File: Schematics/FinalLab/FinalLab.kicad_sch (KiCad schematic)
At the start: 0 parts

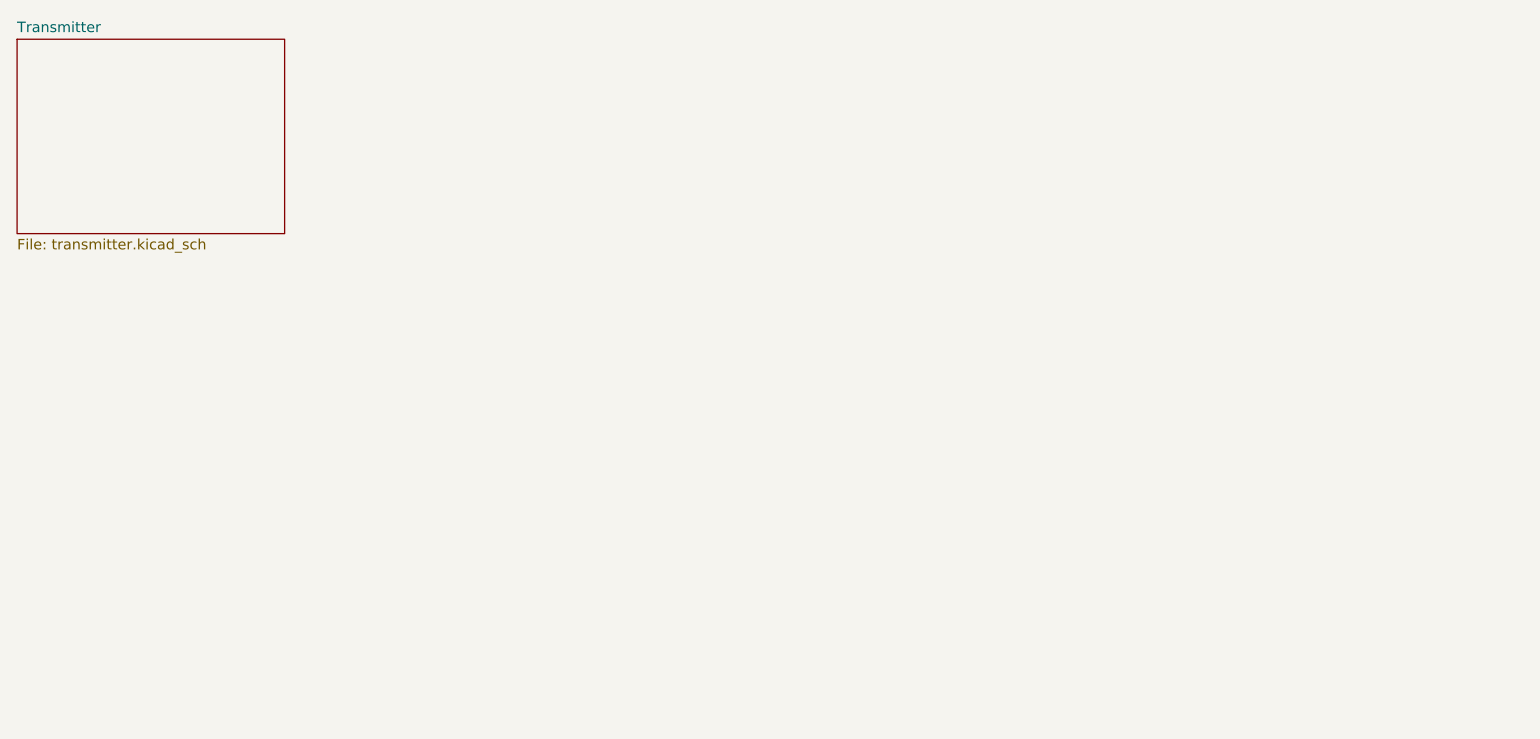
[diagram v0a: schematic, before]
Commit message: WIP
Labview is being worked on, schematic is complete, report is almost done. We need reciever code with PID stuff.
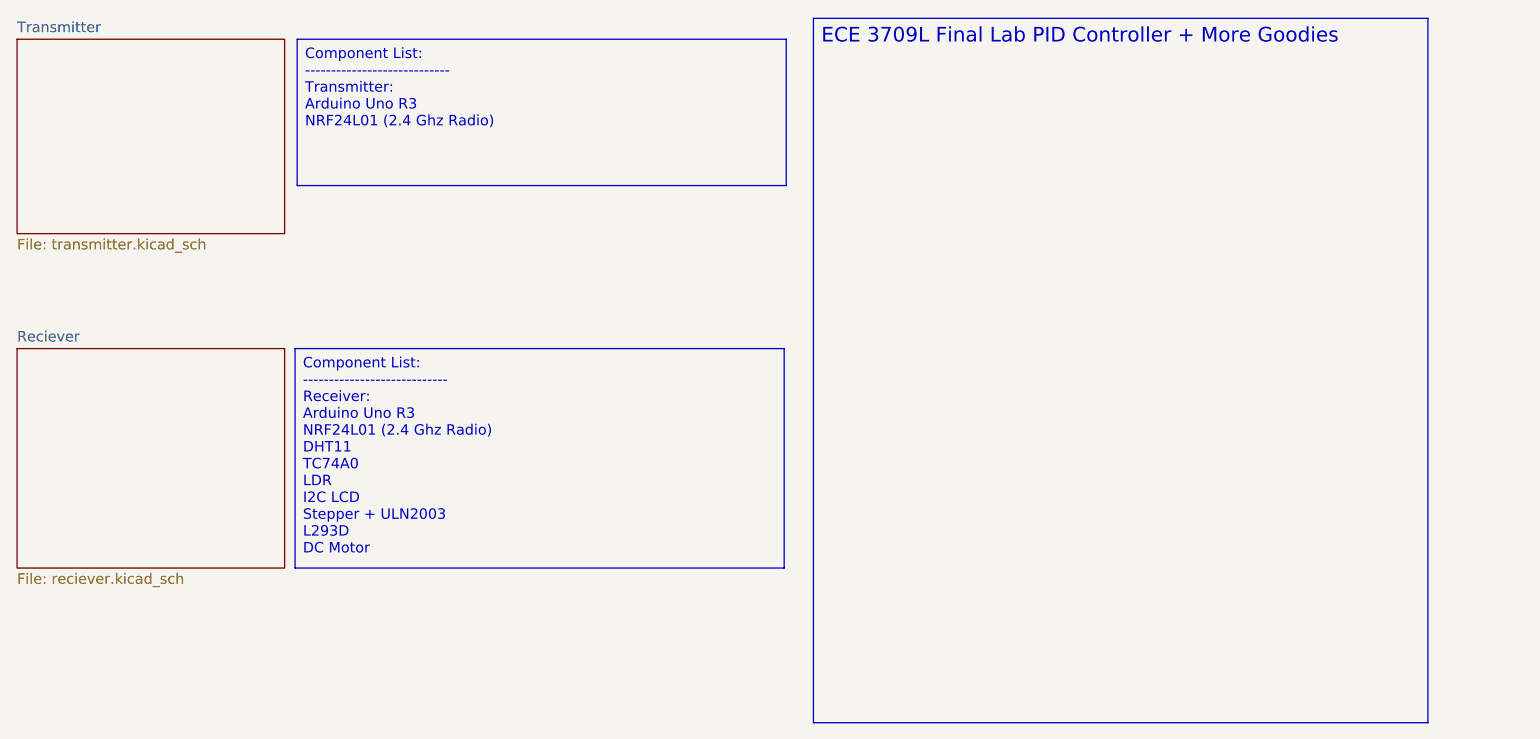
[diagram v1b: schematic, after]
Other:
- added sheet Reciever (reciever.kicad_sch)

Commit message: updating
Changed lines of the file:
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@@
 		)
 	)
-	(text_box "Component List:\n----------------------------\nReceiver:\nArduino Uno R3\nNRF24L01 (2.4 Ghz Radio)\nDHT11\nTC74A0\nLDR\nI2C LCD\nStepper + ULN2003\nL293D\nDC Motor"
+	(text_box "Component List:\n----------------------------\nReceiver:\nArduino Uno R3\nNRF24L01 (2.4 Ghz Radio)\nDHT11\nLDR\nI2C LCD\nL293D\nDC Motor"
 		(exclude_from_sim no)
 		(at 57.15 55.88 0)
